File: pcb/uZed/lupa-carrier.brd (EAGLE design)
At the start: 101.9 x 57.1 mm, 43 parts, among them K1 694108105102

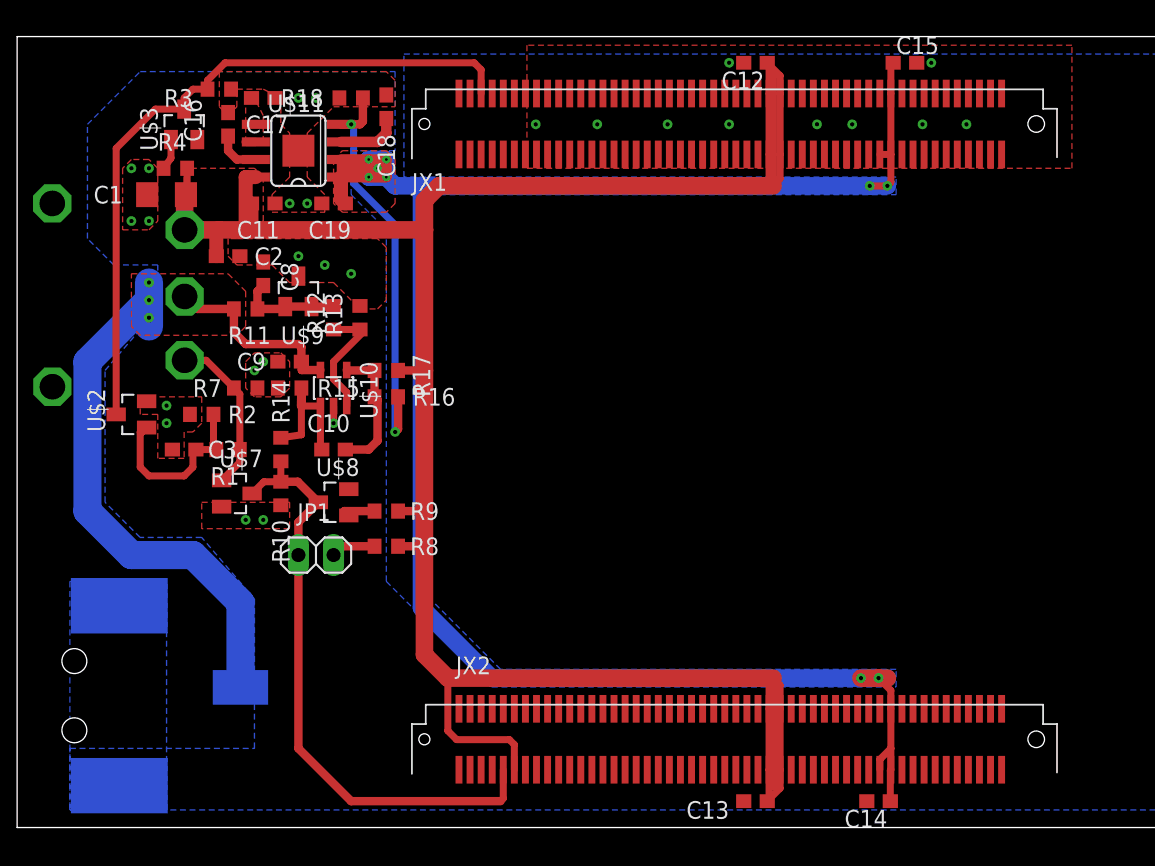
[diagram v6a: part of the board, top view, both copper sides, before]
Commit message: arranged silk screen text.
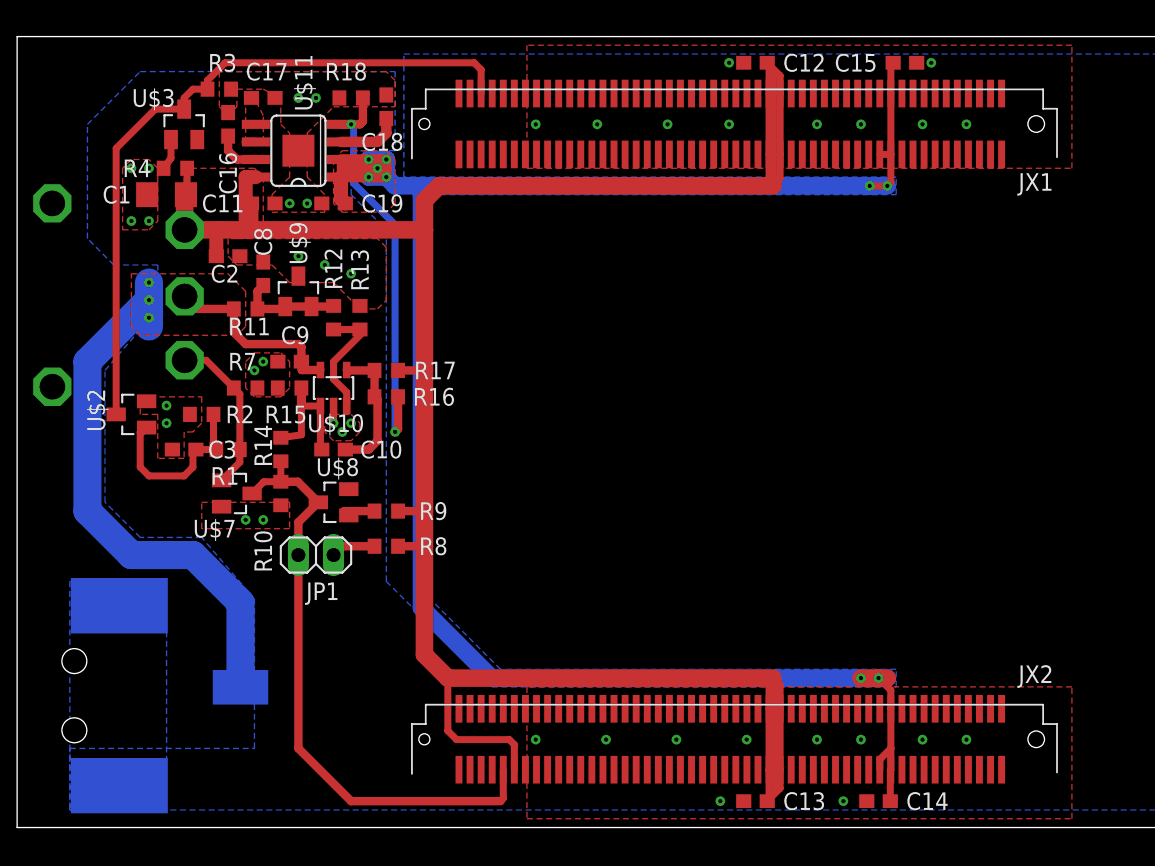
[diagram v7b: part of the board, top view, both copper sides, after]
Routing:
- net GND: vias 28 -> 40

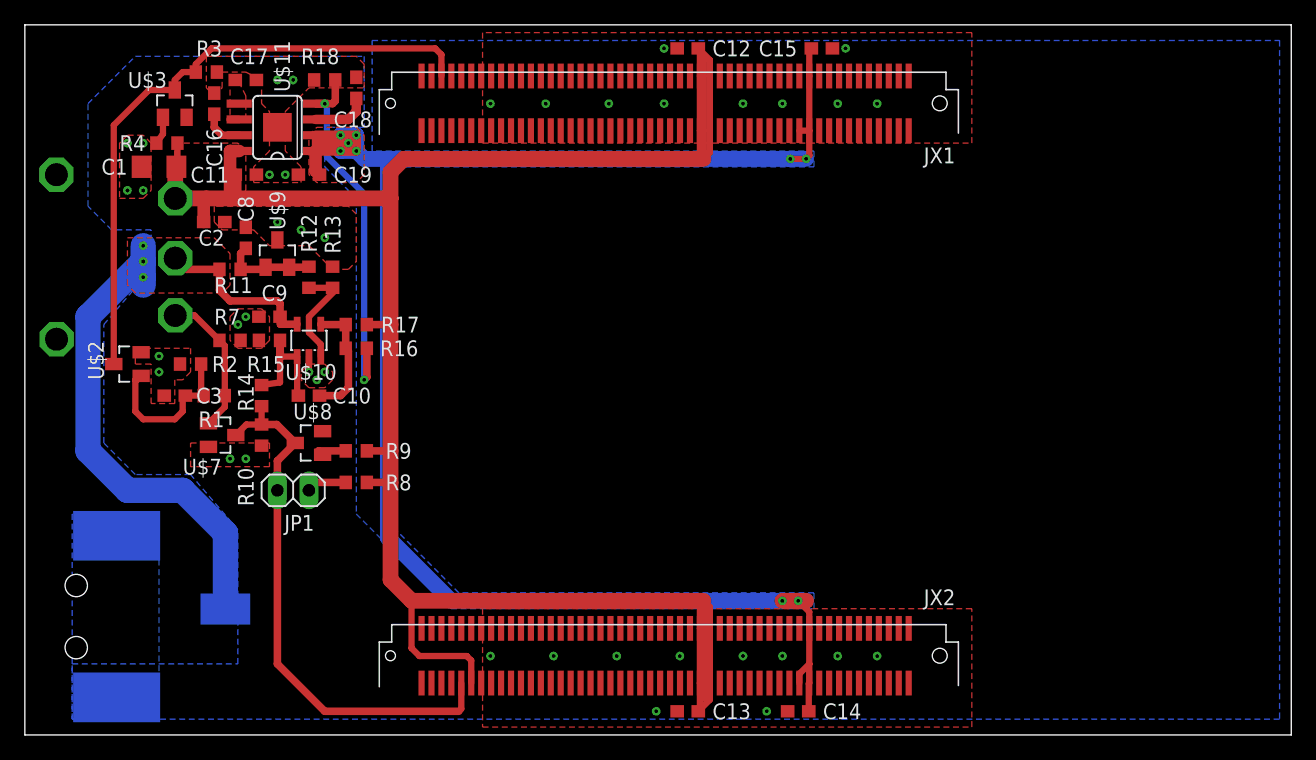
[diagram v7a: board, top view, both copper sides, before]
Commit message: ordered 5 from pcbway as is
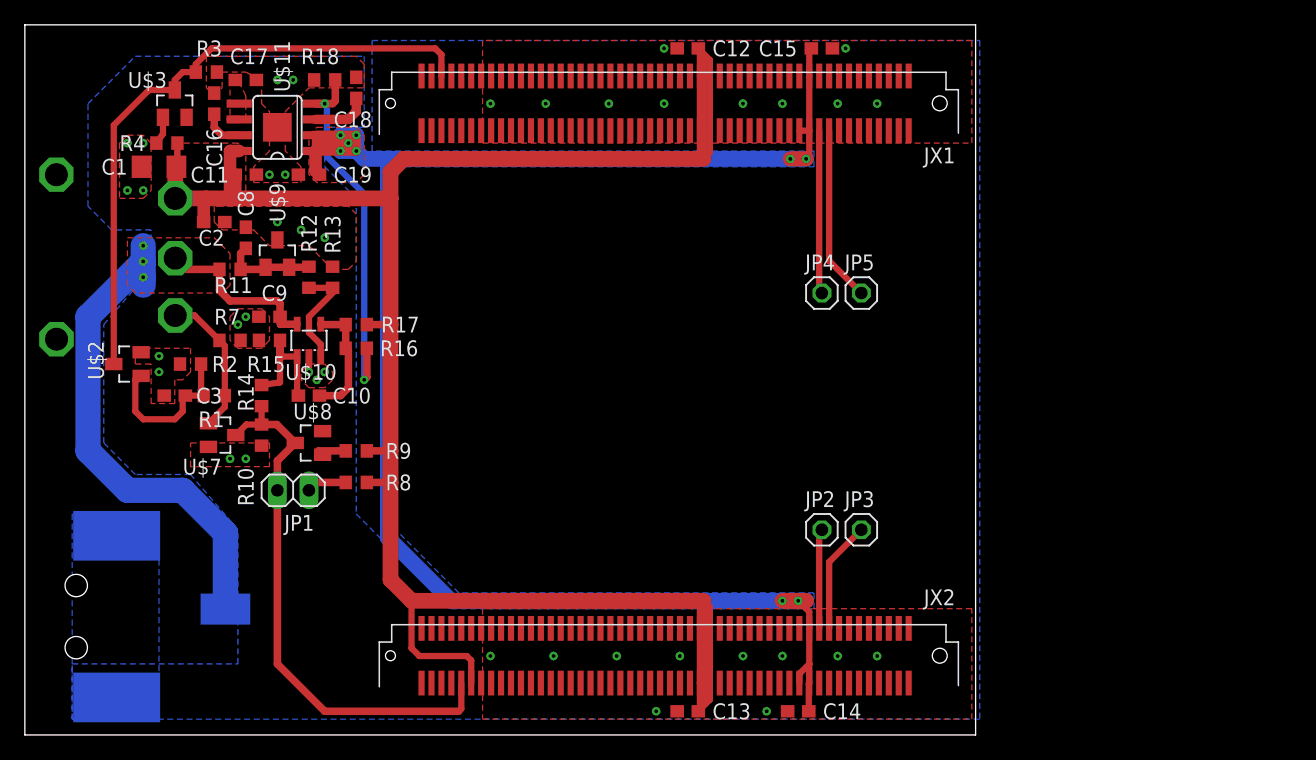
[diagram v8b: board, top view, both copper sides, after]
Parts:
- added JP2, JP3, JP4, JP5: (no value), pinhead:1X01
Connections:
- new net N$13: JP2.1, JX2.P$20
- new net N$14: JP3.1, JX2.P$18
- new net N$15: JP4.1, JX1.P$19
- new net N$16: JP5.1, JX1.P$17
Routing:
- net N$16: track 0.00 -> 14.1 mm
- net N$15: track 0.00 -> 13.2 mm
- net N$14: track 0.00 -> 9.01 mm
- net N$13: track 0.00 -> 8.02 mm
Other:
- board size 101.9 x 57.1 mm -> 76.5 x 57.1 mm
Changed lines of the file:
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@@
 <layer number="23" name="tOrigins" color="15" fill="1" visible="yes" active="yes"/>
 <layer number="24" name="bOrigins" color="15" fill="1" visible="yes" active="yes"/>
-<layer number="25" name="tNames" color="7" fill="1" visible="yes" active="yes"/>
+<layer number="25" name="tNames" color="7" fill="1" visible="no" active="yes"/>
 <layer number="26" name="bNames" color="7" fill="1" visible="yes" active="yes"/>
 <layer number="27" name="tValues" color="7" fill="1" visible="yes" active="yes"/>
@@
 <board>
 <plain>
-<wire x1="0" y1="0" x2="101.905" y2="0" width="0" layer="20"/>
-<wire x1="101.905" y1="0" x2="101.905" y2="57.14" width="0" layer="20"/>
-<wire x1="101.905" y1="57.14" x2="0" y2="57.14" width="0" layer="20"/>
+<wire x1="0" y1="0" x2="76.505" y2="0" width="0" layer="20"/>
+<wire x1="76.505" y1="0" x2="76.505" y2="57.14" width="0" layer="20"/>
+<wire x1="76.505" y1="57.14" x2="0" y2="57.14" width="0" layer="20"/>
 <wire x1="0" y1="57.14" x2="0" y2="0" width="0" layer="20"/>
 </plain>
@@
 </element>
 <element name="C8" library="rcl" library_urn="urn:adsk.eagle:library:334" package="C0603" package3d_urn="urn:adsk.eagle:package:23616/2" value=".1uF" x="17.78" y="40.005" smashed="yes" rot="R90">
-<attribute name="NAME" x="18.415" y="41.275" size="1.27" layer="25" rot="R90"/>
+<attribute name="NAME" x="17.145" y="43.815" size="1.27" layer="25" rot="R270"/>
 <attribute name="SPICEPREFIX" value="C" x="17.78" y="40.005" size="1.778" layer="27" rot="R90" display="off"/>
 </element>
 <element name="U$9" library="lupa300-components" package="SOT23" value="TL431A" x="20.32" y="38.735" smashed="yes">
-<attribute name="NAME" x="20.955" y="40.64" size="1.27" layer="25" rot="R90"/>
+<attribute name="NAME" x="20.955" y="41.275" size="1.27" layer="25" rot="R90"/>
 </element>
 <element name="R11" library="rcl" library_urn="urn:adsk.eagle:library:334" package="R0603" package3d_urn="urn:adsk.eagle:package:23555/2" value="1k" x="16.51" y="37.465" smashed="yes">
@@
 <attribute name="SPICEPREFIX" value="C" x="22.86" y="45.085" size="1.778" layer="27" rot="R180" display="off"/>
 </element>
+<element name="JP2" library="pinhead" library_urn="urn:adsk.eagle:library:325" package="1X01" package3d_urn="urn:adsk.eagle:package:22485/2" value="" x="64.135" y="16.51"/>
+<element name="JP3" library="pinhead" library_urn="urn:adsk.eagle:library:325" package="1X01" package3d_urn="urn:adsk.eagle:package:22485/2" value="" x="67.31" y="16.51"/>
+<element name="JP4" library="pinhead" library_urn="urn:adsk.eagle:library:325" package="1X01" package3d_urn="urn:adsk.eagle:package:22485/2" value="" x="64.135" y="35.56"/>
+<element name="JP5" library="pinhead" library_urn="urn:adsk.eagle:library:325" package="1X01" package3d_urn="urn:adsk.eagle:package:22485/2" value="" x="67.31" y="35.56"/>
 </elements>
 <signals>
@@
 <vertex x="27.94" y="46.99"/>
 <vertex x="27.94" y="55.88"/>
-<vertex x="100.965" y="55.88"/>
-<vertex x="100.965" y="1.27"/>
+<vertex x="76.835" y="55.88"/>
+<vertex x="76.835" y="1.27"/>
 <vertex x="3.81" y="1.27"/>
 <vertex x="3.81" y="5.715"/>
@@
 <vertex x="36.83" y="47.625"/>
 <vertex x="76.2" y="47.625"/>
-<vertex x="76.2" y="56.515"/>
-<vertex x="36.83" y="56.515"/>
+<vertex x="76.2" y="55.88"/>
+<vertex x="36.83" y="55.88"/>
 </polygon>
 <via x="37.465" y="50.8" extent="1-16" drill="0.3"/>
@@
 </polygon>
 <polygon width="0.1524" layer="1" isolate="0.2032" orphans="yes" thermals="no">
-<vertex x="36.83" y="0.635"/>
-<vertex x="76.2" y="0.635"/>
+<vertex x="36.83" y="1.27"/>
+<vertex x="76.2" y="1.27"/>
 <vertex x="76.2" y="10.16"/>
 <vertex x="36.83" y="10.16"/>
@@
 <vertex x="22.86" y="48.26"/>
 </polygon>
-<wire x1="61.595" y1="46.355" x2="62.865" y2="46.355" width="0.508" layer="1"/>
+<wire x1="61.595" y1="46.355" x2="62.865" y2="46.355" width="1.2192" layer="1"/>
 </signal>
 <signal name="PG_CARRIER">
@@
 <wire x1="54.61" y1="10.16" x2="54.61" y2="3.175" width="1.016" layer="1"/>
 </signal>
+<signal name="N$13">
+<contactref element="JP2" pad="1"/>
+<contactref element="JX2" pad="P$20"/>
+<wire x1="63.92" y1="8.575" x2="63.92" y2="16.295" width="0.508" layer="1"/>
+<wire x1="63.92" y1="16.295" x2="64.135" y2="16.51" width="0.508" layer="1"/>
+</signal>
+<signal name="N$14">
+<contactref element="JP3" pad="1"/>
+<contactref element="JX2" pad="P$18"/>
+<wire x1="64.72" y1="8.575" x2="64.72" y2="13.92" width="0.508" layer="1"/>
+<wire x1="64.72" y1="13.92" x2="67.31" y2="16.51" width="0.508" layer="1"/>
+</signal>
+<signal name="N$15">
+<contactref element="JP4" pad="1"/>
+<contactref element="JX1" pad="P$19"/>
+<wire x1="63.92" y1="48.625" x2="63.92" y2="35.775" width="0.508" layer="1"/>
+<wire x1="63.92" y1="35.775" x2="64.135" y2="35.56" width="0.508" layer="1"/>
+</signal>
+<signal name="N$16">
+<contactref element="JP5" pad="1"/>
+<contactref element="JX1" pad="P$17"/>
+<wire x1="64.72" y1="48.625" x2="64.72" y2="38.15" width="0.508" layer="1"/>
+<wire x1="64.72" y1="38.15" x2="67.31" y2="35.56" width="0.508" layer="1"/>
+</signal>
 </signals>
